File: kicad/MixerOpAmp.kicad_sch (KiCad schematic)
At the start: 13 parts, among them U5 TL072

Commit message: saved
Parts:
- renumbered C2 to C10, C1 to C9
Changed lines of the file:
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@@
   (symbol (lib_id "Device:C") (at 78.74 173.99 0) (unit 1)
     (in_bom yes) (on_board yes) (dnp no) (fields_autoplaced)
-    (property "Reference" "C2" (at 82.55 172.72 0)
+    (property "Reference" "C10" (at 82.55 172.72 0)
       (effects (font (size 1.27 1.27)) (justify left))
     )
@@
     (instances
       (project "Tiny4xPoweredStereoMixer"
-        (path "/68c4b081-ef47-4ba5-a55f-4ef66cb2b598/f21b05ca-c53e-4c9f-92f9-42535cdfa7f7"
-          (reference "C2") (unit 1)
-        )
-        (path "/68c4b081-ef47-4ba5-a55f-4ef66cb2b598/552f3912-3928-454a-823e-6f183577fda8"
-          (reference "C8") (unit 1)
-        )
-        (path "/68c4b081-ef47-4ba5-a55f-4ef66cb2b598/4f5d350b-a08e-4f50-b16f-b5f92c91b503"
+        (path "/68c4b081-ef47-4ba5-a55f-4ef66cb2b598/4d0e0b63-01b4-4976-9c90-722e772b5af2"
           (reference "C10") (unit 1)
         )
-        (path "/68c4b081-ef47-4ba5-a55f-4ef66cb2b598/bfd1c0ad-a46f-412b-810b-077847d96983"
-          (reference "C12") (unit 1)
-        )
-        (path "/68c4b081-ef47-4ba5-a55f-4ef66cb2b598/4d0e0b63-01b4-4976-9c90-722e772b5af2"
-          (reference "C10") (unit 1)
-        )
       )
     )
@@
   (symbol (lib_id "power:-12V") (at 78.74 167.64 0) (unit 1)
     (in_bom yes) (on_board yes) (dnp no) (fields_autoplaced)
-    (property "Reference" "#PWR04" (at 78.74 165.1 0)
+    (property "Reference" "#PWR025" (at 78.74 165.1 0)
       (effects (font (size 1.27 1.27)) hide)
     )
@@
     (instances
       (project "Tiny4xPoweredStereoMixer"
-        (path "/68c4b081-ef47-4ba5-a55f-4ef66cb2b598/f21b05ca-c53e-4c9f-92f9-42535cdfa7f7"
-          (reference "#PWR04") (unit 1)
-        )
-        (path "/68c4b081-ef47-4ba5-a55f-4ef66cb2b598/552f3912-3928-454a-823e-6f183577fda8"
-          (reference "#PWR011") (unit 1)
-        )
-        (path "/68c4b081-ef47-4ba5-a55f-4ef66cb2b598/4f5d350b-a08e-4f50-b16f-b5f92c91b503"
-          (reference "#PWR016") (unit 1)
-        )
-        (path "/68c4b081-ef47-4ba5-a55f-4ef66cb2b598/bfd1c0ad-a46f-412b-810b-077847d96983"
-          (reference "#PWR021") (unit 1)
-        )
         (path "/68c4b081-ef47-4ba5-a55f-4ef66cb2b598/4d0e0b63-01b4-4976-9c90-722e772b5af2"
           (reference "#PWR025") (unit 1)
@@
   (symbol (lib_id "Device:C") (at 66.04 173.99 0) (unit 1)
     (in_bom yes) (on_board yes) (dnp no) (fields_autoplaced)
-    (property "Reference" "C1" (at 69.85 172.72 0)
+    (property "Reference" "C9" (at 69.85 172.72 0)
       (effects (font (size 1.27 1.27)) (justify left))
     )
@@
     (instances
       (project "Tiny4xPoweredStereoMixer"
-        (path "/68c4b081-ef47-4ba5-a55f-4ef66cb2b598/f21b05ca-c53e-4c9f-92f9-42535cdfa7f7"
-          (reference "C1") (unit 1)
-        )
-        (path "/68c4b081-ef47-4ba5-a55f-4ef66cb2b598/552f3912-3928-454a-823e-6f183577fda8"
-          (reference "C7") (unit 1)
-        )
-        (path "/68c4b081-ef47-4ba5-a55f-4ef66cb2b598/4f5d350b-a08e-4f50-b16f-b5f92c91b503"
+        (path "/68c4b081-ef47-4ba5-a55f-4ef66cb2b598/4d0e0b63-01b4-4976-9c90-722e772b5af2"
           (reference "C9") (unit 1)
         )
-        (path "/68c4b081-ef47-4ba5-a55f-4ef66cb2b598/bfd1c0ad-a46f-412b-810b-077847d96983"
-          (reference "C11") (unit 1)
-        )
-        (path "/68c4b081-ef47-4ba5-a55f-4ef66cb2b598/4d0e0b63-01b4-4976-9c90-722e772b5af2"
-          (reference "C9") (unit 1)
-        )
       )
     )
@@
   (symbol (lib_id "power:+12V") (at 66.04 167.64 0) (unit 1)
     (in_bom yes) (on_board yes) (dnp no) (fields_autoplaced)
-    (property "Reference" "#PWR03" (at 66.04 171.45 0)
+    (property "Reference" "#PWR023" (at 66.04 171.45 0)
       (effects (font (size 1.27 1.27)) hide)
     )
@@
     (instances
       (project "Tiny4xPoweredStereoMixer"
-        (path "/68c4b081-ef47-4ba5-a55f-4ef66cb2b598/f21b05ca-c53e-4c9f-92f9-42535cdfa7f7"
-          (reference "#PWR03") (unit 1)
-        )
-        (path "/68c4b081-ef47-4ba5-a55f-4ef66cb2b598/552f3912-3928-454a-823e-6f183577fda8"
-          (reference "#PWR09") (unit 1)
-        )
-        (path "/68c4b081-ef47-4ba5-a55f-4ef66cb2b598/4f5d350b-a08e-4f50-b16f-b5f92c91b503"
-          (reference "#PWR014") (unit 1)
-        )
-        (path "/68c4b081-ef47-4ba5-a55f-4ef66cb2b598/bfd1c0ad-a46f-412b-810b-077847d96983"
-          (reference "#PWR019") (unit 1)
-        )
         (path "/68c4b081-ef47-4ba5-a55f-4ef66cb2b598/4d0e0b63-01b4-4976-9c90-722e772b5af2"
           (reference "#PWR023") (unit 1)
@@
   (symbol (lib_id "power:GND") (at 72.39 182.88 0) (unit 1)
     (in_bom yes) (on_board yes) (dnp no) (fields_autoplaced)
-    (property "Reference" "#PWR05" (at 72.39 189.23 0)
+    (property "Reference" "#PWR024" (at 72.39 189.23 0)
       (effects (font (size 1.27 1.27)) hide)
     )
@@
     (instances
       (project "Tiny4xPoweredStereoMixer"
-        (path "/68c4b081-ef47-4ba5-a55f-4ef66cb2b598/f21b05ca-c53e-4c9f-92f9-42535cdfa7f7"
-          (reference "#PWR05") (unit 1)
-        )
-        (path "/68c4b081-ef47-4ba5-a55f-4ef66cb2b598/552f3912-3928-454a-823e-6f183577fda8"
-          (reference "#PWR010") (unit 1)
-        )
-        (path "/68c4b081-ef47-4ba5-a55f-4ef66cb2b598/4f5d350b-a08e-4f50-b16f-b5f92c91b503"
-          (reference "#PWR015") (unit 1)
-        )
-        (path "/68c4b081-ef47-4ba5-a55f-4ef66cb2b598/bfd1c0ad-a46f-412b-810b-077847d96983"
-          (reference "#PWR020") (unit 1)
-        )
         (path "/68c4b081-ef47-4ba5-a55f-4ef66cb2b598/4d0e0b63-01b4-4976-9c90-722e772b5af2"
           (reference "#PWR024") (unit 1)

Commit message: completed reva layout
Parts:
- C10, C9: Mouser (none) -> 791-0603B104J250CT
- R1, R10, R2, R3, R4, R5, R6, R7, R8, R9: Mouser (none) -> 71-CRCW080510K0FKEAC
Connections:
- net ch1_left_mix_in: now also R4.1; no longer R1.1
- net ch1_right_mix_in: now also R8.1; no longer R5.1
- net ch2_left_mix_in: now also R3.1; no longer R2.1
- net ch2_right_mix_in: now also R7.1; no longer R6.1
- net ch3_left_mix_in: now also R2.1; no longer R3.1
- net ch3_right_mix_in: now also R6.1; no longer R7.1
- net ch4_left_mix_in: now also R1.1; no longer R4.1
- net ch4_right_mix_in: now also R5.1; no longer R8.1
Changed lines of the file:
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@@
     (stroke (width 0) (type default))
   )
-  (hierarchical_label "ch4_left_mix_in" (shape input) (at 88.9 67.31 180) (fields_autoplaced)
+  (hierarchical_label "ch4_left_mix_in" (shape input) (at 88.9 40.64 180) (fields_autoplaced)
     (effects (font (size 1.27 1.27)) (justify right))
   )
@@
     (effects (font (size 1.27 1.27)) (justify left))
   )
-  (hierarchical_label "ch1_right_mix_in" (shape input) (at 88.9 100.33 180) (fields_autoplaced)
-    (effects (font (size 1.27 1.27)) (justify right))
-  )
-  (hierarchical_label "ch4_right_mix_in" (shape input) (at 88.9 127 180) (fields_autoplaced)
-    (effects (font (size 1.27 1.27)) (justify right))
-  )
-  (hierarchical_label "ch3_right_mix_in" (shape input) (at 88.9 118.11 180) (fields_autoplaced)
+  (hierarchical_label "ch1_right_mix_in" (shape input) (at 88.9 127 180) (fields_autoplaced)
+    (effects (font (size 1.27 1.27)) (justify right))
+  )
+  (hierarchical_label "ch4_right_mix_in" (shape input) (at 88.9 100.33 180) (fields_autoplaced)
+    (effects (font (size 1.27 1.27)) (justify right))
+  )
+  (hierarchical_label "ch3_right_mix_in" (shape input) (at 88.9 109.22 180) (fields_autoplaced)
     (effects (font (size 1.27 1.27)) (justify right))
   )
@@
     (effects (font (size 1.27 1.27)) (justify left))
   )
-  (hierarchical_label "ch2_right_mix_in" (shape input) (at 88.9 109.22 180) (fields_autoplaced)
-    (effects (font (size 1.27 1.27)) (justify right))
-  )
-  (hierarchical_label "ch3_left_mix_in" (shape input) (at 88.9 58.42 180) (fields_autoplaced)
-    (effects (font (size 1.27 1.27)) (justify right))
-  )
-  (hierarchical_label "ch1_left_mix_in" (shape input) (at 88.9 40.64 180) (fields_autoplaced)
-    (effects (font (size 1.27 1.27)) (justify right))
-  )
-  (hierarchical_label "ch2_left_mix_in" (shape input) (at 88.9 49.53 180) (fields_autoplaced)
+  (hierarchical_label "ch2_right_mix_in" (shape input) (at 88.9 118.11 180) (fields_autoplaced)
+    (effects (font (size 1.27 1.27)) (justify right))
+  )
+  (hierarchical_label "ch3_left_mix_in" (shape input) (at 88.9 49.53 180) (fields_autoplaced)
+    (effects (font (size 1.27 1.27)) (justify right))
+  )
+  (hierarchical_label "ch1_left_mix_in" (shape input) (at 88.9 67.31 180) (fields_autoplaced)
+    (effects (font (size 1.27 1.27)) (justify right))
+  )
+  (hierarchical_label "ch2_left_mix_in" (shape input) (at 88.9 58.42 180) (fields_autoplaced)
     (effects (font (size 1.27 1.27)) (justify right))
   )
@@
       (effects (font (size 1.27 1.27)) hide)
     )
-    (property "Mouser" "" (at 97.79 67.31 0)
+    (property "Mouser" "71-CRCW080510K0FKEAC" (at 97.79 67.31 0)
       (effects (font (size 1.27 1.27)) hide)
     )
@@
       (effects (font (size 1.27 1.27)) hide)
     )
-    (property "Mouser" "" (at 78.74 173.99 0)
+    (property "Mouser" "791-0603B104J250CT" (at 78.74 173.99 0)
       (effects (font (size 1.27 1.27)) hide)
     )
@@
       (effects (font (size 1.27 1.27)) hide)
     )
-    (property "Mouser" "" (at 97.79 49.53 0)
+    (property "Mouser" "71-CRCW080510K0FKEAC" (at 97.79 49.53 0)
       (effects (font (size 1.27 1.27)) hide)
     )
@@
       (effects (font (size 1.27 1.27)) hide)
     )
-    (property "Mouser" "" (at 158.75 54.61 0)
+    (property "Mouser" "71-CRCW080510K0FKEAC" (at 158.75 54.61 0)
       (effects (font (size 1.27 1.27)) hide)
     )
@@
       (effects (font (size 1.27 1.27)) hide)
     )
-    (property "Mouser" "" (at 97.79 127 0)
+    (property "Mouser" "71-CRCW080510K0FKEAC" (at 97.79 127 0)
       (effects (font (size 1.27 1.27)) hide)
     )
@@
       (effects (font (size 1.27 1.27)) hide)
     )
-    (property "Mouser" "" (at 66.04 173.99 0)
+    (property "Mouser" "791-0603B104J250CT" (at 66.04 173.99 0)
       (effects (font (size 1.27 1.27)) hide)
     )
@@
       (effects (font (size 1.27 1.27)) hide)
     )
-    (property "Mouser" "" (at 97.79 118.11 0)
+    (property "Mouser" "71-CRCW080510K0FKEAC" (at 97.79 118.11 0)
       (effects (font (size 1.27 1.27)) hide)
     )
@@
       (effects (font (size 1.27 1.27)) hide)
     )
-    (property "Mouser" "" (at 97.79 100.33 0)
+    (property "Mouser" "71-CRCW080510K0FKEAC" (at 97.79 100.33 0)
       (effects (font (size 1.27 1.27)) hide)
     )
@@
       (effects (font (size 1.27 1.27)) hide)
     )
-    (property "Mouser" "" (at 97.79 40.64 0)
+    (property "Mouser" "71-CRCW080510K0FKEAC" (at 97.79 40.64 0)
       (effects (font (size 1.27 1.27)) hide)
     )
@@
       (effects (font (size 1.27 1.27)) hide)
     )
-    (property "Mouser" "" (at 97.79 58.42 0)
+    (property "Mouser" "71-CRCW080510K0FKEAC" (at 97.79 58.42 0)
       (effects (font (size 1.27 1.27)) hide)
     )
@@
       (effects (font (size 1.27 1.27)) hide)
     )
-    (property "Mouser" "" (at 158.75 114.3 0)
+    (property "Mouser" "71-CRCW080510K0FKEAC" (at 158.75 114.3 0)
       (effects (font (size 1.27 1.27)) hide)
     )
@@
       (effects (font (size 1.27 1.27)) hide)
     )
-    (property "Mouser" "" (at 97.79 109.22 0)
-      (effects (font (size 1.27 1.27)) hide)
-    )
+    (property "Mouser" "71-CRCW080510K0FKEAC" (at 97.79 109.22 0)
+      (effects (font (size 1.27 1.27)) hide)
+    )

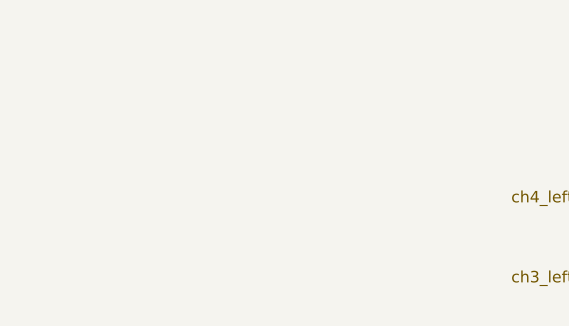
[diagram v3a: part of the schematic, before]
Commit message: -  Fixed in-rush current problem using soft-start design. https://github.com/cracked-machine/Tiny4xPoweredStereoMixer/issues/4 - Fixed reversed pots. https://github.com/cracked-machine/Tiny4xPoweredStereoMixer/issues/3 - Made more space surrounding pwr in connector. https://github.com/cracked-machine/Tiny4xPoweredStereoMixer/issues/8
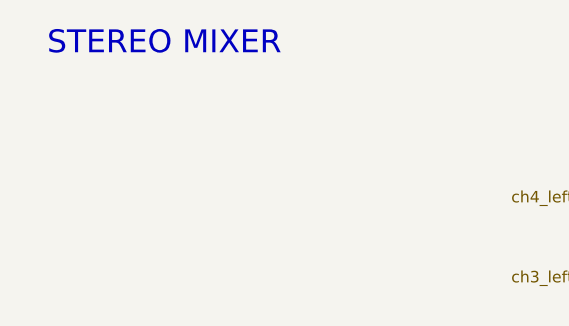
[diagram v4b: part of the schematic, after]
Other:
- note added: "STEREO MIXER"
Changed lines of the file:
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@@
 	(generator_version "8.0")
 	(paper "A4")
+	(title_block
+		(rev "B")
+	)
 	(junction
 		(at 72.39 181.61)
@@
 			(width 0)
 			(type default)
+		)
+	)
+	(text "STEREO MIXER"
+		(exclude_from_sim no)
+		(at 35.306 23.622 0)
+		(effects
+			(font
+				(size 2.54 2.54)
+			)
 		)
 	)
@@
 			)
 		)
-		(property "Description" ""
+		(property "Description" "Dual Low-Noise JFET-Input Operational Amplifiers, DIP-8/SOIC-8"
 			(at 113.03 175.26 0)
 			(effects
@@
 			)
 		)
-		(property "Datasheet" "https://datasheet.lcsc.com/lcsc/2206010216_UNI-ROYAL-Uniroyal-Elec-0805W8F1002T5E_C17414.pdf"
+		(property "Datasheet" "~"
 			(at 97.79 67.31 0)
 			(effects
@@
 			)
 		)
-		(property "Description" ""
+		(property "Description" "Resistor"
 			(at 97.79 67.31 0)
 			(effects
@@
 			)
 		)
-		(property "Datasheet" "https://datasheet.lcsc.com/lcsc/2304140030_Samsung-Electro-Mechanics-CL10B104KA8NNNC_C1590.pdf"
+		(property "Datasheet" "~"
 			(at 78.74 173.99 0)
 			(effects
@@
 			)
 		)
-		(property "Description" ""
+		(property "Description" "Unpolarized capacitor"
 			(at 78.74 173.99 0)
 			(effects
@@
 			)
 		)
-		(property "Description" ""
+		(property "Description" "Power symbol creates a global label with name \"GND\" , ground"
 			(at 147.32 138.43 0)
 			(effects
@@
 			)
 		)
-		(property "Datasheet" "https://datasheet.lcsc.com/lcsc/2206010216_UNI-ROYAL-Uniroyal-Elec-0805W8F1002T5E_C17414.pdf"
+		(property "Datasheet" "~"
 			(at 97.79 49.53 0)
 			(effects
@@
 			)
 		)
-		(property "Description" ""
+		(property "Description" "Resistor"
 			(at 97.79 49.53 0)
 			(effects
@@
 			)
 		)
-		(property "Description" ""
+		(property "Description" "Power symbol creates a global label with name \"-12V\""
 			(at 78.74 167.64 0)
 			(effects
@@
 			)
 		)
-		(property "Description" ""
+		(property "Description" "Power symbol creates a global label with name \"GND\" , ground"
 			(at 147.32 78.74 0)
 			(effects
@@
 			)
 		)
-		(property "Description" ""
+		(property "Description" "Dual Low-Noise JFET-Input Operational Amplifiers, DIP-8/SOIC-8"
 			(at 160.02 129.54 0)
 			(effects
@@
 			)
 		)
-		(property "Description" ""
+		(property "Description" "Power symbol creates a global label with name \"-12V\""
 			(at 110.49 184.15 0)
 			(effects
@@
 			)
 		)
-		(property "Description" ""
+		(property "Description" "Power symbol creates a global label with name \"+12V\""
 			(at 110.49 165.1 0)
 			(effects
@@
 			)
 		)
-		(property "Datasheet" "https://datasheet.lcsc.com/lcsc/2206010216_UNI-ROYAL-Uniroyal-Elec-0805W8F1002T5E_C17414.pdf"
+		(property "Datasheet" "~"
 			(at 158.75 54.61 0)
 			(effects
@@
 			)
 		)
-		(property "Description" ""
+		(property "Description" "Resistor"
 			(at 158.75 54.61 0)
 			(effects
@@
 			)
 		)
-		(property "Datasheet" "https://datasheet.lcsc.com/lcsc/2206010216_UNI-ROYAL-Uniroyal-Elec-0805W8F1002T5E_C17414.pdf"
+		(property "Datasheet" "~"
 			(at 97.79 127 0)
 			(effects
@@
 			)
 		)
-		(property "Description" ""
+		(property "Description" "Resistor"
 			(at 97.79 127 0)
 			(effects
@@
 			)
 		)
-		(property "Datasheet" "https://datasheet.lcsc.com/lcsc/2304140030_Samsung-Electro-Mechanics-CL10B104KA8NNNC_C1590.pdf"
+		(property "Datasheet" "~"
 			(at 66.04 173.99 0)
 			(effects
@@
 			)
 		)
-		(property "Description" ""
+		(property "Description" "Unpolarized capacitor"
 			(at 66.04 173.99 0)
 			(effects
@@
 			)
 		)
-		(property "Datasheet" "https://datasheet.lcsc.com/lcsc/2206010216_UNI-ROYAL-Uniroyal-Elec-0805W8F1002T5E_C17414.pdf"
+		(property "Datasheet" "~"
 			(at 97.79 118.11 0)
 			(effects
@@
 			)
 		)
-		(property "Description" ""
+		(property "Description" "Resistor"
 			(at 97.79 118.11 0)
 			(effects
@@
 			)
 		)
-		(property "Description" ""
+		(property "Description" "Power symbol creates a global label with name \"+12V\""
 			(at 66.04 167.64 0)
 			(effects
@@
 			)
 		)
-		(property "Description" ""
+		(property "Description" "Dual Low-Noise JFET-Input Operational Amplifiers, DIP-8/SOIC-8"
 			(at 160.02 69.85 0)
 			(effects
@@
 			)
 		)
-		(property "Datasheet" "https://datasheet.lcsc.com/lcsc/2206010216_UNI-ROYAL-Uniroyal-Elec-0805W8F1002T5E_C17414.pdf"
+		(property "Datasheet" "~"
 			(at 97.79 100.33 0)
 			(effects
@@
 			)
 		)
-		(property "Description" ""
+		(property "Description" "Resistor"
 			(at 97.79 100.33 0)
 			(effects
@@
 			)
 		)
-		(property "Datasheet" "https://datasheet.lcsc.com/lcsc/2206010216_UNI-ROYAL-Uniroyal-Elec-0805W8F1002T5E_C17414.pdf"
+		(property "Datasheet" "~"
 			(at 97.79 40.64 0)
 			(effects
@@
 			)
 		)
-		(property "Description" ""
+		(property "Description" "Resistor"
 			(at 97.79 40.64 0)
 			(effects
@@
 			)
 		)
-		(property "Datasheet" "https://datasheet.lcsc.com/lcsc/2206010216_UNI-ROYAL-Uniroyal-Elec-0805W8F1002T5E_C17414.pdf"
+		(property "Datasheet" "~"
 			(at 97.79 58.42 0)
 			(effects
@@
 			)
 		)
-		(property "Description" ""
+		(property "Description" "Resistor"
 			(at 97.79 58.42 0)
 			(effects
@@
 			)
 		)
-		(property "Datasheet" "https://datasheet.lcsc.com/lcsc/2206010216_UNI-ROYAL-Uniroyal-Elec-0805W8F1002T5E_C17414.pdf"
+		(property "Datasheet" "~"
 			(at 158.75 114.3 0)
 			(effects
@@
 			)
 		)
-		(property "Description" ""
+		(property "Description" "Resistor"
 			(at 158.75 114.3 0)
 			(effects
@@
 			)
 		)
-		(property "Description" ""
+		(property "Description" "Power symbol creates a global label with name \"GND\" , ground"
 			(at 72.39 182.88 0)
 			(effects
@@
 			)
 		)
-		(property "Datasheet" "https://datasheet.lcsc.com/lcsc/2206010216_UNI-ROYAL-Uniroyal-Elec-0805W8F1002T5E_C17414.pdf"
+		(property "Datasheet" "~"
 			(at 97.79 109.22 0)
 			(effects
@@
 			)
 		)
-		(property "Description" ""
+		(property "Description" "Resistor"
 			(at 97.79 109.22 0)
 			(effects
